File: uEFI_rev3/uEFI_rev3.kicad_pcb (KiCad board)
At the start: 4 copper layers, 99 x 113 mm, 261 parts, among them J1 USB_B, J2 Tag connect, J3 36638-0002, J4 Conn_02x08_Odd_Even, J5 Conn_01x03, Q1 ISL9V5045S3ST, Q10 IRF540N, Q11 SS8050, Q12 AO3400A, Q13 AO3400A, Q14 AO3400A, Q15 AO3400A, Q16 AO3400A, Q2 ISL9V5045S3ST, Q3 ISL9V5045S3ST, Q4 ISL9V5045S3ST, Q5 SS8050, Q6 IRLZ44N, Q7 IRLZ44N, Q8 SS8050, Q9 SS8050, SW1 SW_Push, U1 MCZ33810EK, U12 OPA340NA, U15 TJA1042T3118, U2 74HC4851, U20 TPL7407LAPWR, U22 TPL7407LAPWR, U23 PaP_Driver_v1, U27 LM321, U3 STM32F407VGTx, U31 LM321, U36 MAX9926UAEE+, U4 MIC2940A-3.3WU, U5 MIC2940A-5.0WT, U6 LT4363IMS, U7 25LCxxx, U9 OPA340NA, Y1 25MHz

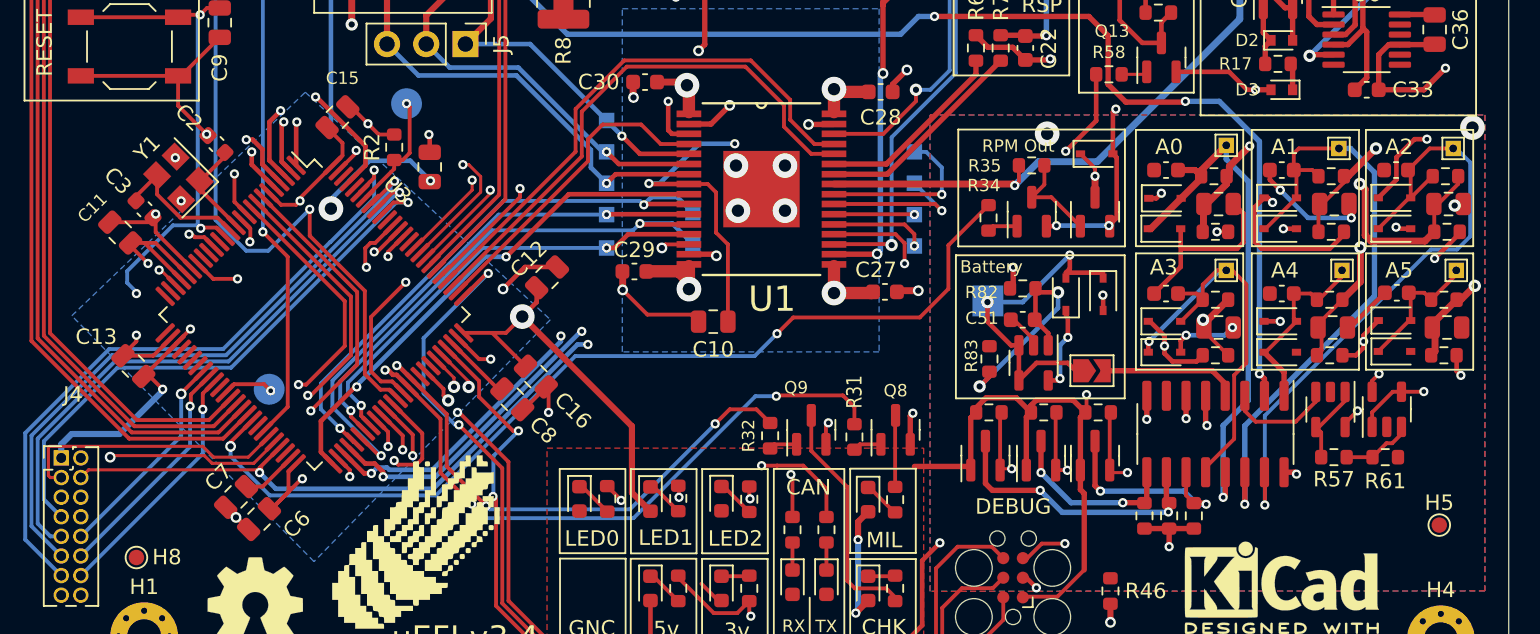
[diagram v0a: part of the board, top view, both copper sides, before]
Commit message: fix bom output
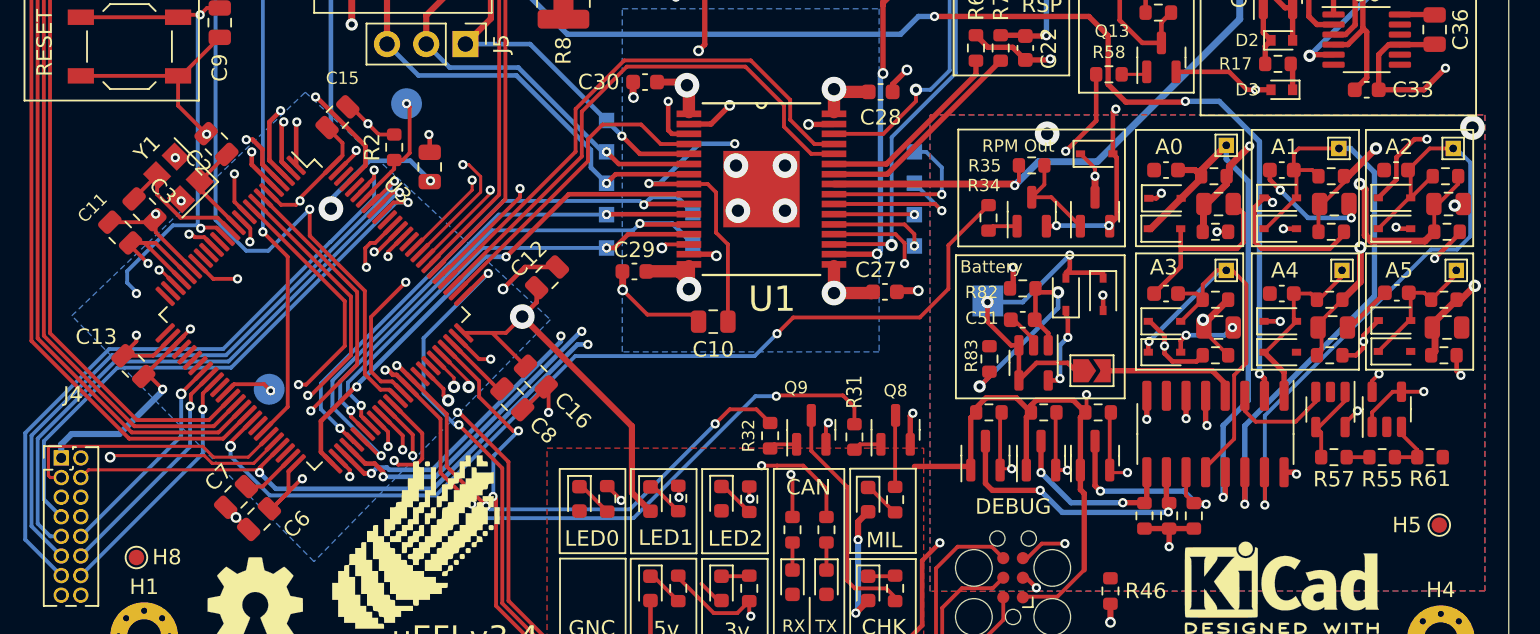
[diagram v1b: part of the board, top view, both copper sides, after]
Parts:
- added R55: 200R, Resistor_SMD:R_0603_1608Metric, F.Cu at (146.0, 140.3)
- C2, C3: footprint Capacitor_SMD:C_0603_1608Metric -> Capacitor_SMD:C_0805_2012Metric
- R121, R122: value R_Small -> 10k
- R57: value 1k7 -> 1k5
- moved R61 2.90 mm to (149.1, 140.3)
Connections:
- R57 pad 1: /Sensores/MUX_3v3 -> Net-(R57-Pad1)
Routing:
- net Net-(R57-Pad1): track 0.00 -> 1.48 mm
- net /Sensores/MUX_3v3: track 4.63 -> 3.84 mm

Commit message: AA wiring, lib&connector update, added eggbug
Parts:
- added G***: LOGO, LOGO, F.Cu at (98.9, 136.9)

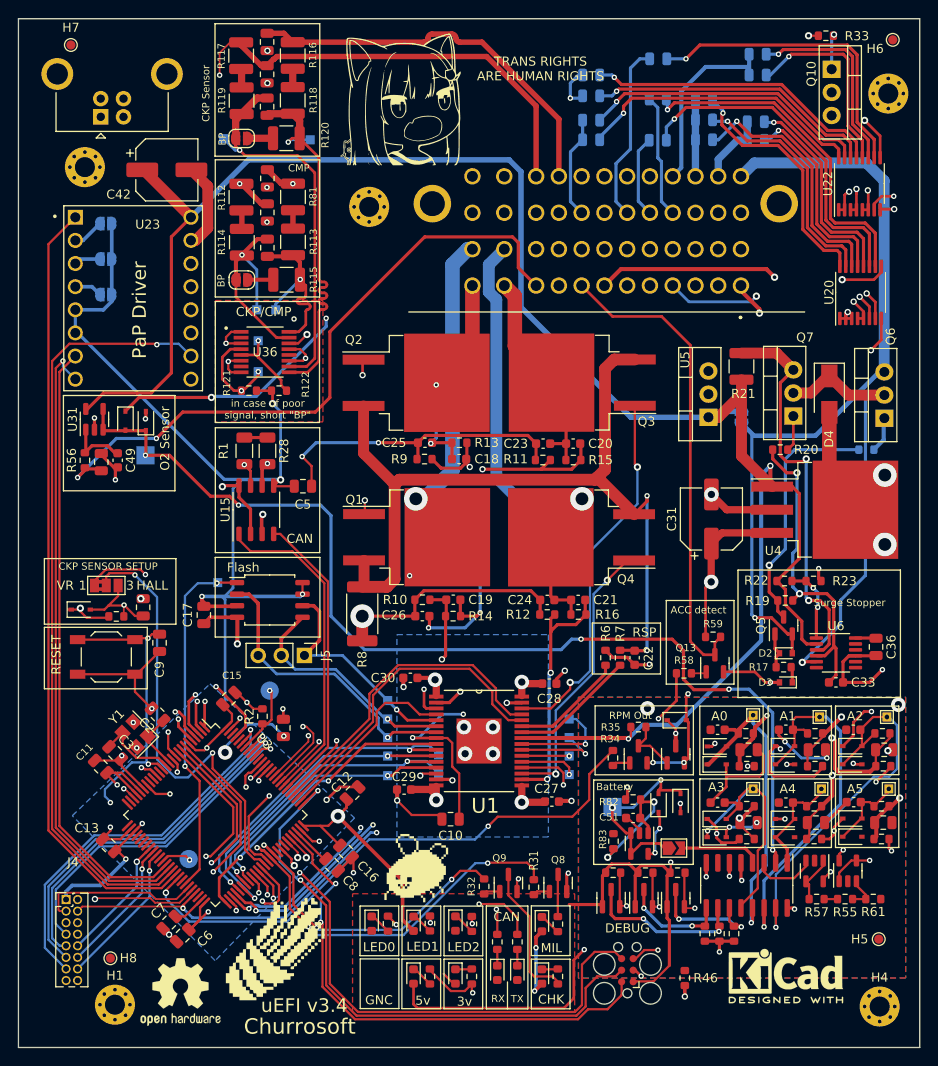
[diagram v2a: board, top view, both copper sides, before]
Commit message: Fix SPI pad & connector, add new images, Co-authored-by: Lucacik <name@example.com>
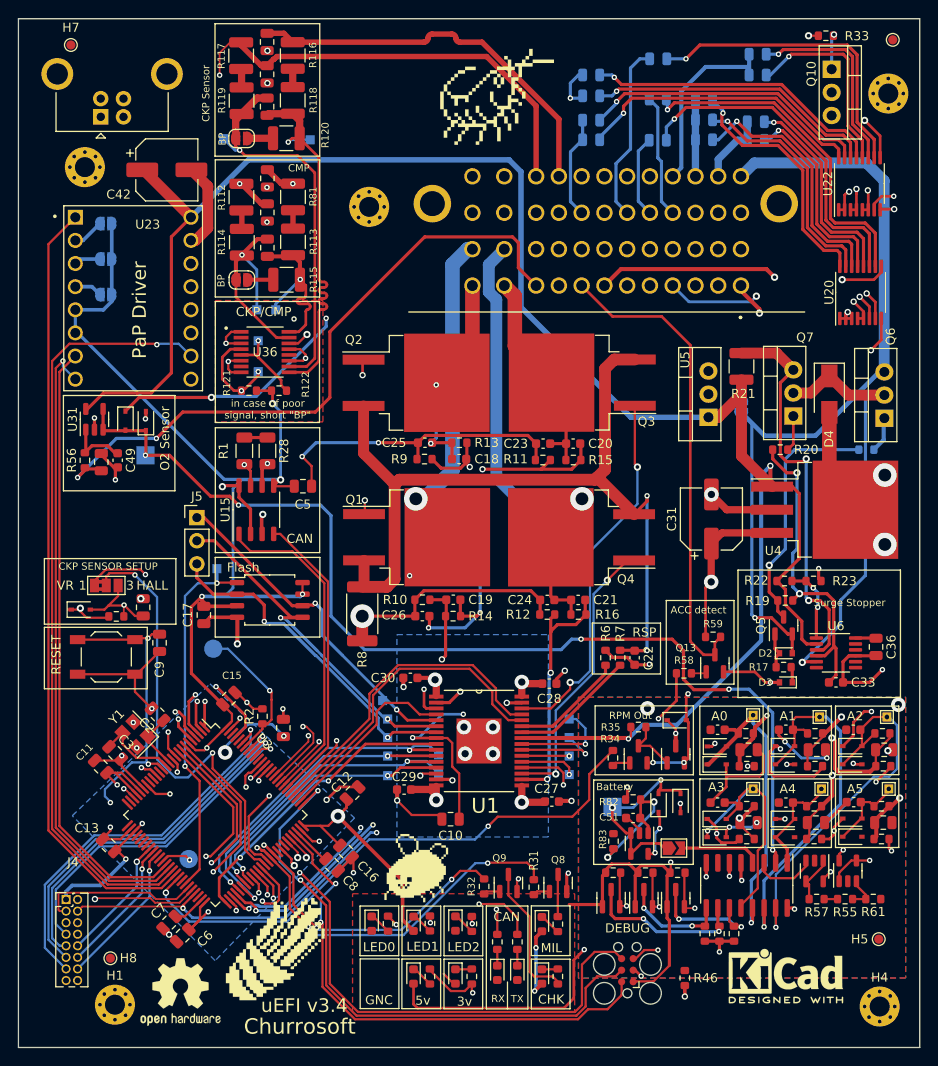
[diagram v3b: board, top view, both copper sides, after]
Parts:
- removed the G*** at (97.5, 52.6)
- removed the G*** at (107.2, 97.0)
- added G***: LOGO, LOGO, F.Cu at (107.8, 52.4)
- added G***: LOGO, LOGO, B.Cu at (104.8, 99.0)
- moved J5 19.2 mm to (74.8, 98.4), turned to 0 degrees
- moved TP1 7.72 mm to (76.6, 112.8)
- moved TP9 1.54 mm to (77.0, 104.0)
- moved JP4 1.18 mm to (134.6, 86.2)
- moved TP28 0.56 mm to (95.2, 118.5)
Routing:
- net /SPI2_MOSI: track 80.4 -> 94.5 mm, vias 3 -> 4
- net /SPI2_SCK: track 79.5 -> 91.8 mm, vias 3 -> 4
- net Net-(R2-Pad1): track 7.71 -> 15.8 mm
- net /SPI2_MISO: track 83.7 -> 88.0 mm, vias 3 -> 4
- net +12VA: track 113.3 -> 115.0 mm
- net /MEMORY_CS: track 39.2 -> 40.8 mm
- net +3V3: track 398.3 -> 399.7 mm
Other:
- board text removed: "TRANS RIGHTS ARE HUMAN RIGHTS"
